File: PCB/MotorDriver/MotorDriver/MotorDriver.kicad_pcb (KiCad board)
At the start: 2 copper layers, 10 parts, among them J1 XT30PW-M, Q5 NMOS, Q6 NMOS, Q7 NMOS, Q8 NMOS, U1 DRV8701ERGET

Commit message: :sparkles: 基板V2完成！！！
MotorDriverになってるけど普通にMain PCB V2ですわ！
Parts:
- added C10: 0.1u, Capacitor_SMD:C_0603_1608Metric_Pad1.08x0.95mm_HandSolder, F.Cu at (96.8, 113.9)
- added C11: 220u, Capacitor_SMD:CP_Elec_10x10, F.Cu at (122.9, 163.1)
- added C12: 1u, Capacitor_SMD:C_0603_1608Metric, F.Cu at (125.5, 147.6)
- added C13: 0.1u, Capacitor_SMD:C_0603_1608Metric_Pad1.08x0.95mm_HandSolder, F.Cu at (110.2, 111.4)
- added C14: 220u, Capacitor_SMD:CP_Elec_6.3x5.4, F.Cu at (109.4, 104.4)
- added C15: 0.1u, Capacitor_SMD:C_0603_1608Metric_Pad1.08x0.95mm_HandSolder, F.Cu at (108.5, 111.4)
- added C16: 0.1u, Capacitor_SMD:C_0603_1608Metric_Pad1.08x0.95mm_HandSolder, F.Cu at (69.5, 164.7)
- added C17: 0.1u, Capacitor_SMD:C_0603_1608Metric, F.Cu at (122.3, 147.6)
- added C18: 0.1u, Capacitor_SMD:C_0603_1608Metric_Pad1.08x0.95mm_HandSolder, F.Cu at (62.4, 117.3)
- added C19: 0.1u, Capacitor_SMD:C_0603_1608Metric_Pad1.08x0.95mm_HandSolder, F.Cu at (76.7, 151.6)
- added C20: 0.1u, Capacitor_SMD:C_0603_1608Metric_Pad1.08x0.95mm_HandSolder, F.Cu at (103.6, 168.8)
- added C21: 220u, Capacitor_SMD:CP_Elec_10x10, F.Cu at (146.1, 143.5)
- added C4: 0.1u, Capacitor_SMD:C_0603_1608Metric_Pad1.08x0.95mm_HandSolder, F.Cu at (135.1, 110.2)
- added C5: 0.1u, Capacitor_SMD:C_0603_1608Metric_Pad1.08x0.95mm_HandSolder, F.Cu at (119.4, 111.0)
- added C6: 22u, Capacitor_SMD:C_1206_3216Metric_Pad1.33x1.80mm_HandSolder, F.Cu at (117.4, 111.7)
- added C7: 22u, Capacitor_SMD:C_1206_3216Metric_Pad1.33x1.80mm_HandSolder, F.Cu at (113.7, 110.4)
- added C8: 0.1u, Capacitor_SMD:C_0603_1608Metric_Pad1.08x0.95mm_HandSolder, F.Cu at (96.8, 106.7)
- added C9: 0.1u, Capacitor_SMD:C_0603_1608Metric_Pad1.08x0.95mm_HandSolder, F.Cu at (66.8, 140.7)
- added D1: ＧＳ１０１０ＦＬ, Diode_SMD:D_SOD-123F, F.Cu at (121.5, 111.5)
- added D3: D_Schottky, Diode_SMD:D_SOD-323_HandSoldering, F.Cu at (98.7, 106.7)
- added D4: LED, LED_SMD:LED_0603_1608Metric_Pad1.05x0.95mm_HandSolder, F.Cu at (115.7, 120.4)
- added D5: LED, LED_SMD:LED_0603_1608Metric_Pad1.05x0.95mm_HandSolder, F.Cu at (113.8, 120.4)
- added D6: LED, LED_SMD:LED_0603_1608Metric_Pad1.05x0.95mm_HandSolder, F.Cu at (119.3, 127.7)
- added D7: LED, LED_SMD:LED_0603_1608Metric_Pad1.05x0.95mm_HandSolder, F.Cu at (119.4, 155.8)
- added D8: LED, LED_SMD:LED_0603_1608Metric_Pad1.05x0.95mm_HandSolder, F.Cu at (110.0, 120.4)
- added D9: LED, LED_SMD:LED_0603_1608Metric_Pad1.05x0.95mm_HandSolder, F.Cu at (111.9, 120.4)
- added J10: JST-XH, Connector_JST:JST_XH_B3B-XH-A_1x03_P2.50mm_Vertical, F.Cu at (94.3, 168.9)
- added J11: JST-XH, Connector_JST:JST_XH_B4B-XH-A_1x04_P2.50mm_Vertical, F.Cu at (54.6, 130.6)
- added J12: JST-XH, Connector_JST:JST_XH_B4B-XH-A_1x04_P2.50mm_Vertical, F.Cu at (54.6, 143.3)
- added J13: JST-XH, Connector_JST:JST_XH_B3B-XH-A_1x03_P2.50mm_Vertical, F.Cu at (84.2, 168.9)
- added J14: JST-XH, Connector_JST:JST_XH_B4B-XH-A_1x04_P2.50mm_Vertical, F.Cu at (62.2, 156.0)
- added J15: JST-XH, Connector_JST:JST_XH_B3B-XH-A_1x03_P2.50mm_Vertical, F.Cu at (74.0, 168.9)
- added J16: JST-XH, Connector_PinHeader_2.54mm:PinHeader_1x03_P2.54mm_Vertical, B.Cu at (79.4, 130.8)
- added J17: JST-XH, Connector_JST:JST_XH_B4B-XH-A_1x04_P2.50mm_Vertical, F.Cu at (54.6, 110.2)
- added J18: JST-XH, Connector_JST:JST_XH_B4B-XH-A_1x04_P2.50mm_Vertical, F.Cu at (54.6, 156.0)
- added J19: JST-XH, Connector_PinHeader_2.54mm:PinHeader_1x03_P2.54mm_Vertical, B.Cu at (79.4, 133.3)
- added J2: JST-XH, Connector_JST:JST_XH_B3B-XH-A_1x03_P2.50mm_Vertical, F.Cu at (108.1, 160.4)
- added J20: JST-XH, Connector_PinHeader_2.54mm:PinHeader_1x03_P2.54mm_Vertical, B.Cu at (79.4, 135.9)
- added J21: JST-XH, Connector_PinHeader_2.54mm:PinHeader_1x03_P2.54mm_Vertical, B.Cu at (79.4, 138.4)
- added J22: JST-XH, Connector_PinHeader_2.54mm:PinHeader_1x03_P2.54mm_Vertical, B.Cu at (79.4, 141.0)
- added J23: JST-XH, Connector_PinHeader_2.54mm:PinHeader_1x03_P2.54mm_Vertical, B.Cu at (79.4, 143.5)
- added J24: JST-XH, Connector_JST:JST_XH_B2B-XH-A_1x02_P2.50mm_Vertical, F.Cu at (66.4, 168.9)
- added J3: XT30PW-M, Connector_AMASS:AMASS_XT30PW-M_1x02_P2.50mm_Horizontal, F.Cu at (139.3, 111.9)
- added J4: XT30PW-M, Connector_AMASS:AMASS_XT30PW-M_1x02_P2.50mm_Horizontal, F.Cu at (139.3, 160.1)
- added J5: JST-XH, Connector_JST:JST_XH_B3B-XH-A_1x03_P2.50mm_Vertical, F.Cu at (108.1, 154.0)
- added J6: JST-XH, Connector_JST:JST_XH_B2B-XH-A_1x02_P2.50mm_Vertical, F.Cu at (54.6, 122.9)
- added J7: JST-XH, Connector_JST:JST_XH_B4B-XH-A_1x04_P2.50mm_Vertical, F.Cu at (62.2, 143.3)
- added J8: JST-XH, Connector_JST:JST_XH_B4B-XH-A_1x04_P2.50mm_Vertical, F.Cu at (62.2, 130.6)
- added J9: JST-XH, Connector_JST:JST_XH_B3B-XH-A_1x03_P2.50mm_Vertical, F.Cu at (108.1, 166.7)
- added LS1: PKLCS1212E4001-R1, PKLCS1212E4001-R1:PKL, F.Cu at (110.8, 134.2)
- added Q1: TJ60S04M3L, Package_TO_SOT_SMD:TO-252-2, F.Cu at (127.7, 110.4)
- added Q10: NMOS, Package_TO_SOT_SMD:SOT-23, F.Cu at (106.8, 126.0)
- added Q2: NMOS, TPH11006NL:TPH11006NL_SOP Advance_TOS-M, F.Cu at (132.9, 148.1)
- added Q3: NMOS, TPH11006NL:TPH11006NL_SOP Advance_TOS-M, F.Cu at (132.9, 154.4)
- added Q4: NMOS, TPH11006NL:TPH11006NL_SOP Advance_TOS-M, F.Cu at (132.9, 167.1)
- added Q9: NMOS, TPH11006NL:TPH11006NL_SOP Advance_TOS-M, F.Cu at (132.9, 160.8)
- added R10: 1k, Resistor_SMD:R_0603_1608Metric_Pad0.98x0.95mm_HandSolder, F.Cu at (122.8, 127.7)
- added R11: 1k, Resistor_SMD:R_0603_1608Metric_Pad0.98x0.95mm_HandSolder, F.Cu at (122.8, 155.8)
- added R12: 1k, Resistor_SMD:R_0603_1608Metric_Pad0.98x0.95mm_HandSolder, F.Cu at (110.0, 124.2)
- added R13: 1k, Resistor_SMD:R_0603_1608Metric_Pad0.98x0.95mm_HandSolder, F.Cu at (111.9, 124.2)
- added R14: 10k, Resistor_SMD:R_0603_1608Metric_Pad0.98x0.95mm_HandSolder, B.Cu at (70.1, 115.3)
- added R15: 4.7k, Resistor_SMD:R_0402_1005Metric_Pad0.72x0.64mm_HandSolder, B.Cu at (59.7, 143.3)
- added R16: 4.7k, Resistor_SMD:R_0402_1005Metric_Pad0.72x0.64mm_HandSolder, B.Cu at (57.1, 145.8)
- added R17: 4.7k, Resistor_SMD:R_0402_1005Metric_Pad0.72x0.64mm_HandSolder, B.Cu at (57.2, 143.3)
- added R18: 4.7k, Resistor_SMD:R_0402_1005Metric_Pad0.72x0.64mm_HandSolder, B.Cu at (59.7, 158.5)
- added R19: 4.7k, Resistor_SMD:R_0402_1005Metric_Pad0.72x0.64mm_HandSolder, B.Cu at (59.7, 156.0)
- added R2: 10k, Resistor_SMD:R_0603_1608Metric_Pad0.98x0.95mm_HandSolder, F.Cu at (132.8, 110.4)
- added R20: 4.7k, Resistor_SMD:R_0402_1005Metric_Pad0.72x0.64mm_HandSolder, B.Cu at (57.2, 158.5)
- added R21: 4.7k, Resistor_SMD:R_0402_1005Metric_Pad0.72x0.64mm_HandSolder, B.Cu at (57.2, 156.0)
- added R3: 10k, Resistor_SMD:R_0603_1608Metric, F.Cu at (120.4, 151.3)
- added R5: 10k, Resistor_SMD:R_0603_1608Metric_Pad0.98x0.95mm_HandSolder, F.Cu at (110.9, 126.9)
- added R6: 4.7k, Resistor_SMD:R_0402_1005Metric_Pad0.72x0.64mm_HandSolder, B.Cu at (59.7, 145.8)
- added R7: 10k, Resistor_SMD:R_0603_1608Metric_Pad0.98x0.95mm_HandSolder, B.Cu at (70.1, 113.0)
- added R8: 10k, Resistor_SMD:R_0603_1608Metric_Pad0.98x0.95mm_HandSolder, F.Cu at (115.7, 124.2)
- added R9: 1k, Resistor_SMD:R_0603_1608Metric_Pad0.98x0.95mm_HandSolder, F.Cu at (113.8, 124.2)
- added SW1: SW_DPST_x2, Button_Switch_THT:SW_E-Switch_EG1271_SPDT, F.Cu at (130.6, 104.1)
- added SW2: SW_Push, newinov-kicad:SKRPACE010, F.Cu at (67.3, 106.4)
- added SW3: SW_Push, newinov-kicad:SKRPACE010, F.Cu at (103.1, 103.9)
- added U2: DRV8701ERGET, DRV8701ERGET:DRV8701ERGET_NV, F.Cu at (123.4, 151.3)
- added U3: TCA9548APWR, Package_SO:TSSOP-24_4.4x7.8mm_P0.65mm, F.Cu at (62.3, 122.2)
- added U4: Pico, MCU_RaspberryPi_and_Boards:RPi_Pico_SMD_TH, F.Cu at (83.9, 124.3)
- added U5: AZ1117CH-3.3TR, Package_TO_SOT_SMD:SOT-223-3_TabPin2, F.Cu at (117.3, 104.1)
- C1: value ` -> 0.1u
- moved Q5 148.2 mm to (132.9, 139.0), turned to 0 degrees
- moved J1 143.8 mm to (139.2, 132.0), turned to -90 degrees
- moved Q6 139.4 mm to (132.9, 132.7), turned to 180 degrees
- moved Q8 130.6 mm to (132.9, 126.3), turned to 180 degrees
- moved C2 125.4 mm to (125.4, 119.4), turned to 180 degrees
- moved Q7 121.8 mm to (132.9, 120.0), turned to 0 degrees
- moved U1 121.5 mm to (123.4, 123.2), turned to -90 degrees
- moved C1 121.1 mm to (122.2, 119.4), turned to 180 degrees
- moved C3 119.2 mm to (122.9, 134.9), turned to 90 degrees
- moved R1 114.0 mm to (120.3, 123.1), turned to -90 degrees
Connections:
- J1 pad 1: Motor1B -> Motor1A
- J1 pad 2: Motor1A -> Motor1B
- U1 pad 13: /MotorDriveUnit/SLEEP -> +3V3
- U1 pad 14: /MotorDriveUnit/IN2 -> INA2
- U1 pad 15: /MotorDriveUnit/IN1 -> INA1
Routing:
- net +3V3: track 0.00 -> 306.3 mm, vias 0 -> 8
- net ADC2: track 0.00 -> 68.8 mm
- net INB1: track 0.00 -> 64.1 mm
- net INB2: track 0.00 -> 60.5 mm
- net INA1: track 0.00 -> 54.9 mm, vias 0 -> 2
- net INA2: track 0.00 -> 54.5 mm, vias 0 -> 2
- net ADC1: track 0.00 -> 53.2 mm
- net ADC0: track 0.00 -> 49.4 mm
- net SCL3: track 0.00 -> 41.7 mm, vias 0 -> 1
- net Alive_LED: track 0.00 -> 41.3 mm, vias 0 -> 1
- net SCL2: track 0.00 -> 41.2 mm, vias 0 -> 1
- net Debug_LED: track 0.00 -> 40.1 mm, vias 0 -> 1
- net SCL: track 0.00 -> 39.9 mm
- net SDA2: track 0.00 -> 39.6 mm, vias 0 -> 2
- net SDA: track 0.00 -> 37.7 mm
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- added copper zone on F.Cu, net +12V
- added copper zone on F.Cu, net +3V3
- added copper zone on F.Cu, net +BATT
- added copper zone on B.Cu, net GND
- added copper zone on F.Cu, net GND
- added copper zone on F.Cu, net Motor2A
- added copper zone on F.Cu, net Motor2B
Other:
- board outline added: 101.3 x 73.7 mm
- board text added: "+"
- board text added: "+12V"
- board text added: "+3V3"
- board text added: "-"
- board text added: "1"
- board text added: "10"
- board text added: "11"
- board text added: "12"
- board text added: "13"
- board text added: "14"
- board text added: "15"
- board text added: "2"
- board text added: "3"
- board text added: "3V3"
- board text added: "ADC0"
- board text added: "ADC1"
- board text added: "ADC2"
- board text added: "Alive"
- board text added: "CharHan!!"
- board text added: "Debug"
- board text added: "Designed By Daiki Tomioka"
- board text added: "GND"
- board text added: "I2C"
- board text added: "I2C0"
- board text added: "I2C1"
- board text added: "I2C2"
- board text added: "I2C3"
- board text added: "IN"
- board text added: "M1"
- board text added: "M2"
- board text added: "RST"
- board text added: "RX"
- board text added: "S"
- board text added: "SCL"
- board text added: "SDA"
- board text added: "SIG"
- board text added: "SW"
- board text added: "Servo"
- board text added: "TX"
- board text added: "The Yakimeshi Robot"

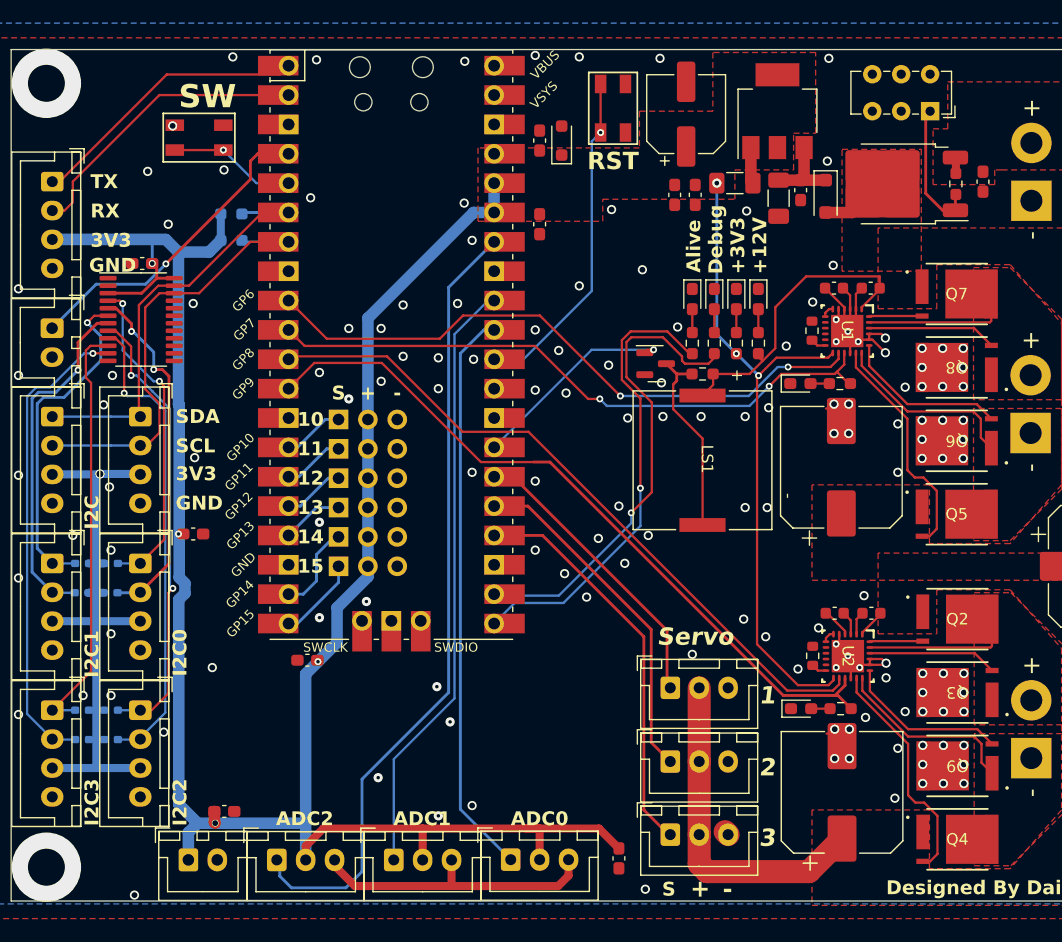
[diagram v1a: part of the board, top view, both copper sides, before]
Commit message: :sparklesビアの追加
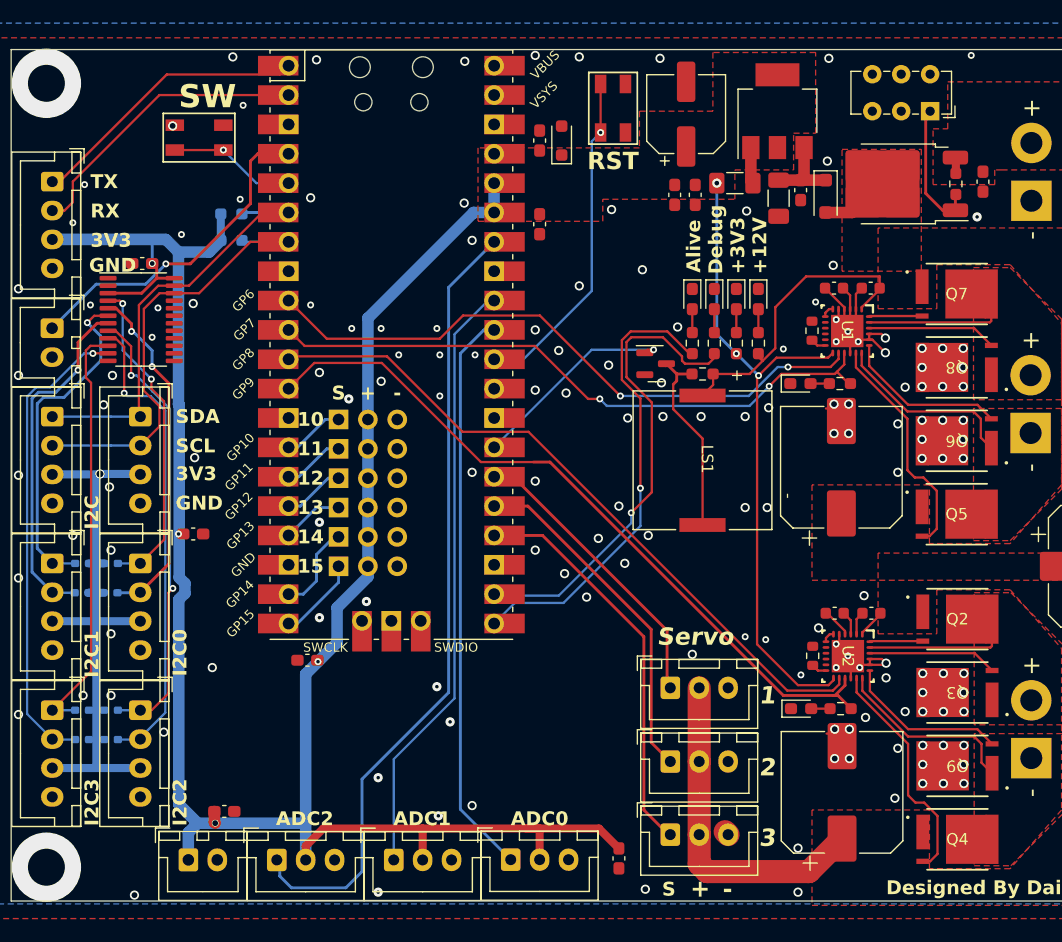
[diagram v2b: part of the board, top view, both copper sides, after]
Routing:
- net GND: track 57.0 -> 32.0 mm, vias 160 -> 170
- net EMG: track 27.6 -> 28.9 mm

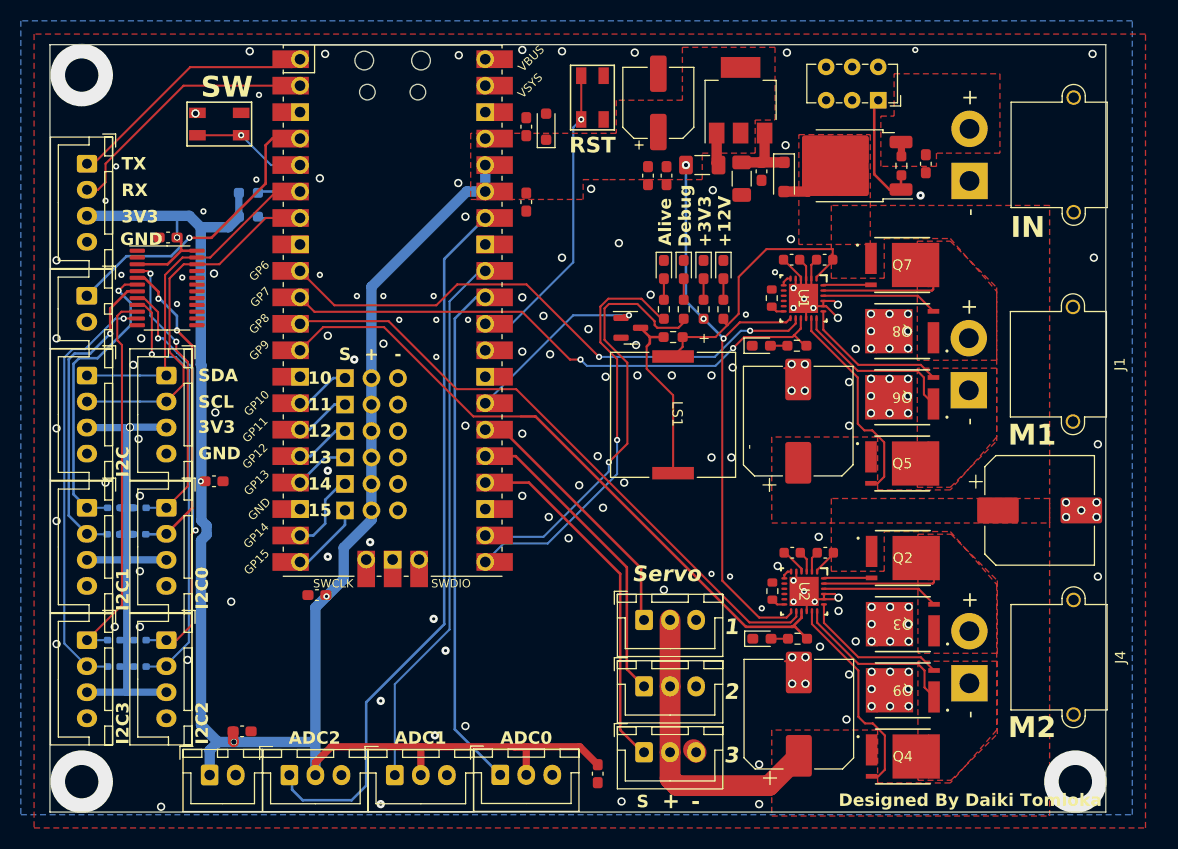
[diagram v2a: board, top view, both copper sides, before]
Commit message: :sparkles: 基板の穴の位置とビアの修正
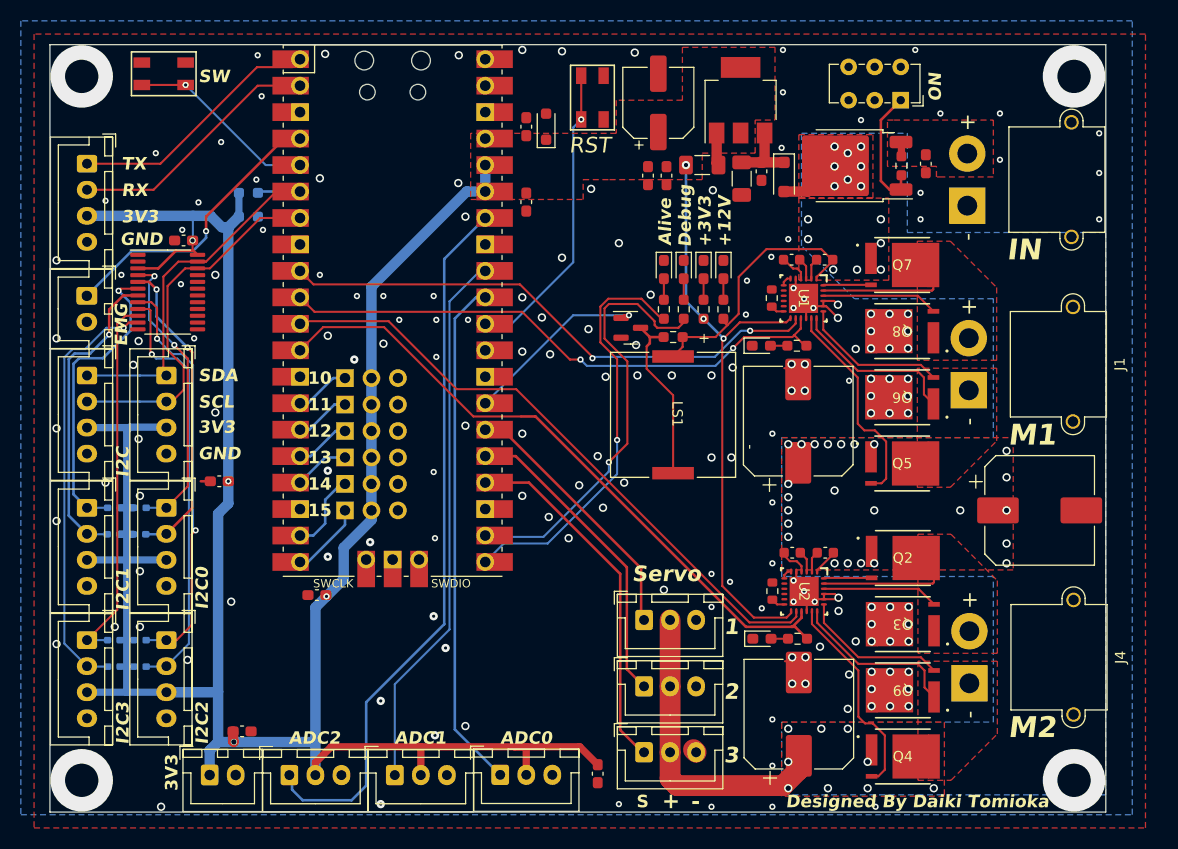
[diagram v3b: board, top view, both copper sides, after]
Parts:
- moved SW2 7.19 mm to (62.0, 101.6)
- moved J3 2.38 mm to (139.1, 114.3)
- moved SW1 2.16 mm to (132.7, 104.1)
- moved C18 1.51 mm to (63.9, 117.6)
- moved C9 0.51 mm to (67.3, 140.7), turned to 180 degrees
- moved U3 0.40 mm to (62.4, 122.6)
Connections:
- J4 pad 1: Motor2B -> Motor2A
- J4 pad 2: Motor2A -> Motor2B
- Q2 pad 3: Motor1B -> Motor2B
- Q3 pad 1: Motor2A -> Motor2B
- Q4 pad 3: Motor1A -> Motor2A
- Q9 pad 1: Motor2B -> Motor2A
- U2 pad 18: Motor2B -> Motor2A
- U2 pad 23: Motor1B -> Motor2B
- U3 pad 1: Net-(U3-A0) -> GND
- U3 pad 2: Net-(U3-A0) -> GND
- U3 pad 21: Net-(U3-A0) -> GND
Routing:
- net Motor2A: track 2.07 -> 17.6 mm
- net Motor1B: track 28.0 -> 15.0 mm
- net SW: track 11.0 -> 18.4 mm
- net +3V3: track 306.3 -> 311.3 mm, vias 8 -> 7
- net Motor2B: track 17.4 -> 15.0 mm
- net INA2: track 54.5 -> 53.0 mm
- net Net-(U1-VCP): track 3.14 -> 2.02 mm
- net Net-(U1-CPH): track 3.18 -> 2.07 mm
- net RX0: track 25.8 -> 24.7 mm
- net EMG: track 28.9 -> 27.9 mm
- net SDA3: track 36.8 -> 35.8 mm
- net Net-(U1-CPL): track 3.62 -> 2.78 mm
- net Net-(Q5-G): track 20.1 -> 20.6 mm
- net GND: track 32.0 -> 32.4 mm, vias 170 -> 180
- net +12V: track 64.9 -> 65.1 mm, vias 0 -> 48
- added copper zone on B.Cu, net +12V
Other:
- board text added: "EMG"
- board text added: "ON"
